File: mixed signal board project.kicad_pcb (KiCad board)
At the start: 4 copper layers, 70.4 x 72.2 mm, 189 parts, among them J101 USB_B_Mini, J102 Conn_01x06_Pin, J201 8P8C_Shielded, J301 Conn_01x04_Pin, J401 AudioJack2_Ground, J402 Conn_01x04_Pin, J403 Screw_Terminal_01x03, J501 USB_B_Mini, J701 Conn_01x02_Socket, J801 Conn_01x02_Socket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

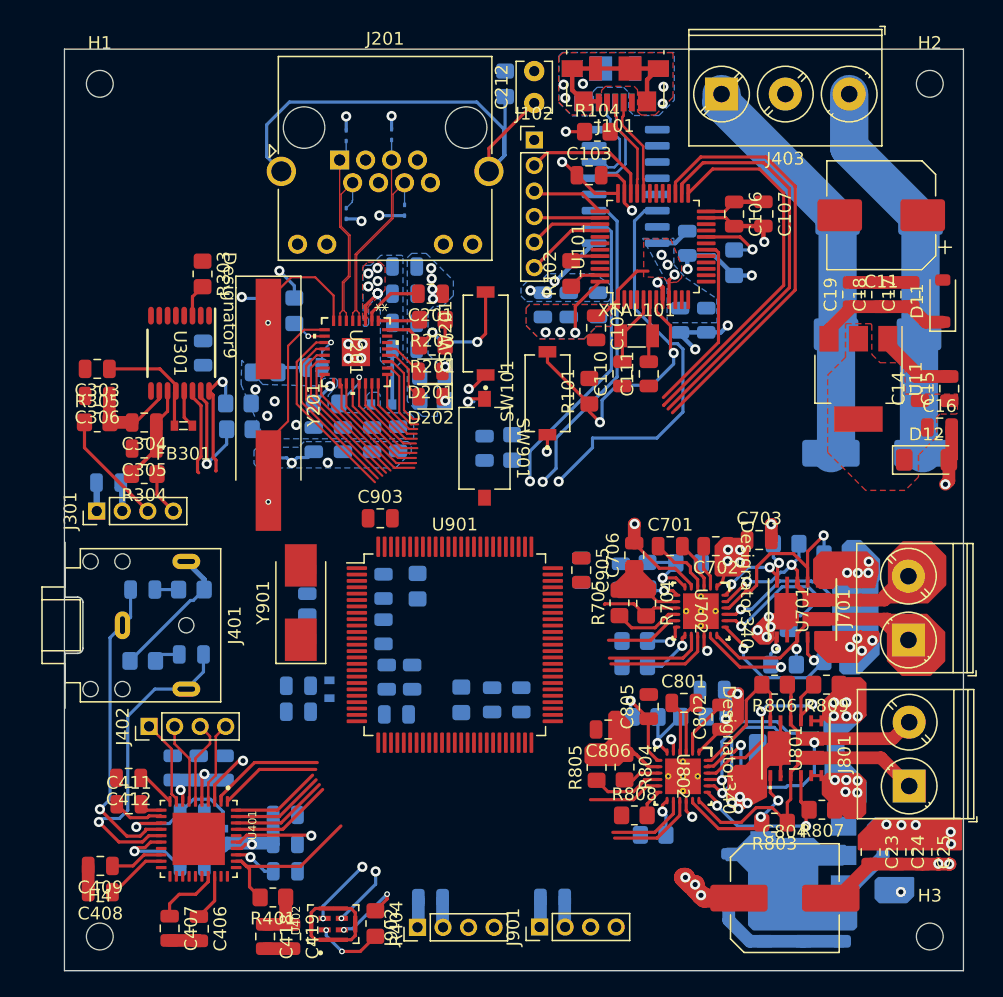
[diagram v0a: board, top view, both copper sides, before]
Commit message: ADC layout reworked, analog and digital ground reworked, other blocks layout have to rework :( ...
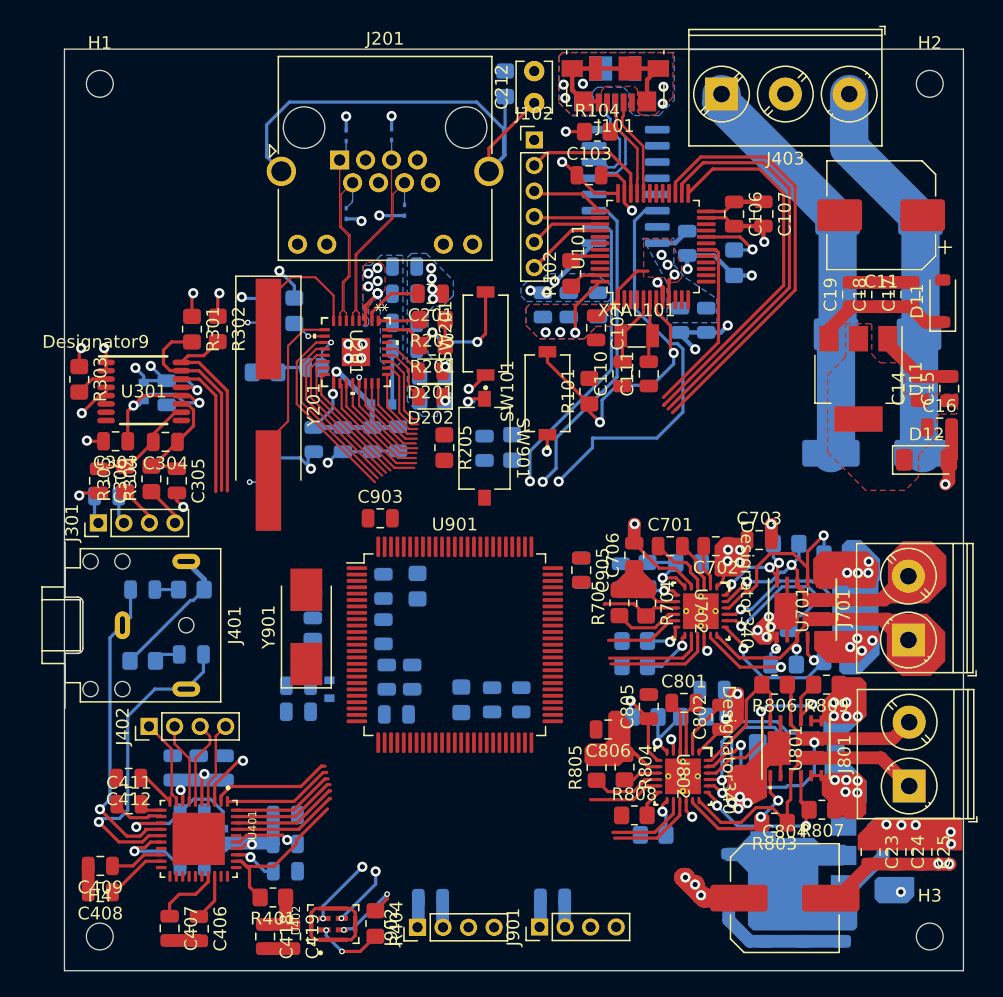
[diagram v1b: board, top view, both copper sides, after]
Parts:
- FB301: moved to B.Cu
- R205, R301, R302: moved to F.Cu
- moved R303 12.7 mm to (84.8, 83.3)
- moved R205 9.89 mm to (113.3, 88.7), turned to -90 degrees
- moved R301 8.68 mm to (93.6, 79.4), turned to -90 degrees
- moved C306 6.65 mm to (86.3, 91.3), turned to -90 degrees
- moved R302 6.06 mm to (95.6, 79.4), turned to -90 degrees
- moved C303 5.85 mm to (87.6, 88.2)
- moved R305 4.94 mm to (88.3, 91.2), turned to 90 degrees
- moved C302 4.22 mm to (91.6, 84.4), turned to -90 degrees
- moved U301 4.13 mm to (89.8, 84.3), turned to 0 degrees
- moved FB301 4.11 mm to (89.8, 84.3), turned to -90 degrees
- moved C305 3.60 mm to (92.4, 91.3), turned to -90 degrees
- moved C304 2.25 mm to (91.5, 88.2)
- moved C913 1.96 mm to (103.0, 104.7)
- moved Y901 1.96 mm to (102.5, 102.7)
- moved C912 1.96 mm to (103.0, 101.1)
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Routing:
- net +3V3: track 64.4 -> 90.1 mm, vias 18 -> 21
- net GND: track 220.2 -> 234.8 mm, vias 46 -> 51
- net /ADC/SDA_ADC: track 9.43 -> 16.8 mm, vias 1 -> 0
- net /ADC/SCK_ADC: track 9.65 -> 15.9 mm, vias 1 -> 0
- net Net-(U301-AVDD): track 9.13 -> 15.1 mm, vias 0 -> 2
- net /ADC/AIN1_ADC: track 9.00 -> 3.24 mm
- net /ADC/~{DRDY}_ADC: track 6.84 -> 10.8 mm
- net /Ethernet/ETH_INT: track 10.4 -> 7.70 mm
- net /Ethernet/ETH_XO: track 10.7 -> 12.3 mm
- net Net-(U301-AIN0): track 7.68 -> 9.08 mm
- net Net-(U301-AIN1): track 7.34 -> 8.63 mm
- net /DAC adn MIC/LRCK_DAC: track 7.12 -> 8.22 mm
- net /DAC adn MIC/SDIN_DAC: track 7.46 -> 8.39 mm
- net /DAC adn MIC/SDA_DAC: track 7.96 -> 8.73 mm
- net /DAC adn MIC/SCLK_DAC: track 7.76 -> 8.44 mm

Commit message: critical nets coloured,some tracks rerouted, section 9 completed.
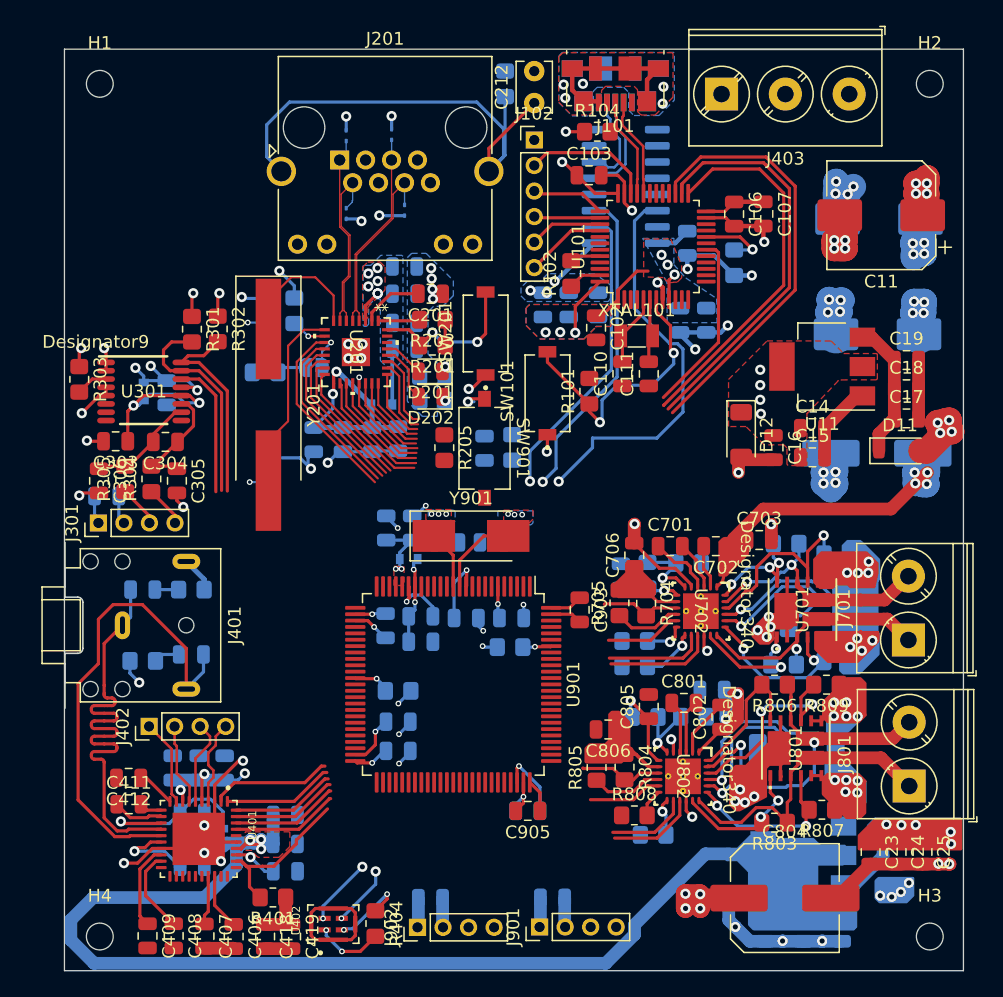
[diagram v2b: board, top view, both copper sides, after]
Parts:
- moved C905 19.3 mm to (119.9, 117.2), turned to 180 degrees
- moved C917 19.3 mm to (119.9, 117.2), turned to 180 degrees
- moved C903 17.2 mm to (124.0, 101.4), turned to -90 degrees
- moved C902 16.0 mm to (108.8, 95.0), turned to 90 degrees
- moved C901 15.2 mm to (110.8, 95.0), turned to 90 degrees
- moved C912 14.9 mm to (117.1, 96.1), turned to 0 degrees
- moved Y901 14.7 mm to (115.4, 95.6), turned to 0 degrees
- moved D12 14.7 mm to (136.6, 87.7), turned to -90 degrees
- moved C913 13.5 mm to (113.5, 96.1), turned to 180 degrees
- moved C16 13.1 mm to (139.1, 88.7), turned to -90 degrees
- moved D11 12.2 mm to (149.1, 89.0), turned to 0 degrees
- moved C15 12.0 mm to (142.2, 89.5), turned to 0 degrees
- moved FB901 11.9 mm to (110.6, 97.4), turned to 0 degrees
- moved C910 10.4 mm to (109.7, 112.5), turned to 0 degrees
- moved C904 10.3 mm to (118.6, 102.0), turned to 0 degrees
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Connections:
- C901 pad 1: Net-(U901-VDDA) -> /STM32F407/VDDA
- C902 pad 1: Net-(U901-VDDA) -> /STM32F407/VDDA
- FB901 pad 1: Net-(U901-VDDA) -> /STM32F407/VDDA
- U702 pad 25: (no net) -> GND
- U802 pad 25: (no net) -> GND
- U901 pad 21: +3V3 -> /STM32F407/VDDA
- U901 pad 22: Net-(U901-VDDA) -> /STM32F407/VDDA
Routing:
- net +1V8: track 9.39 -> 84.9 mm, vias 1 -> 3
- net +3V3: track 90.1 -> 117.7 mm, vias 21 -> 32
- net +12V: track 59.0 -> 80.4 mm, vias 18 -> 38
- net GND: track 234.8 -> 252.0 mm, vias 51 -> 85
- net Net-(U401-HP/LINE_OUTA): track 24.5 -> 37.8 mm, vias 1 -> 0
- net Net-(U401-HP/LINE_OUTB): track 24.2 -> 37.4 mm, vias 1 -> 0
- net Net-(U901-PH0): track 0.00 -> 6.65 mm, vias 0 -> 3
- net Net-(U901-VCAP_2): track 0.00 -> 5.52 mm, vias 0 -> 1
- net /STM32F407/VDDA: track 0.00 -> 5.11 mm, vias 0 -> 2
- net Net-(U901-PH1): track 0.00 -> 4.58 mm, vias 0 -> 3
- net Net-(U901-VCAP_1): track 0.00 -> 4.08 mm, vias 0 -> 1
- net /Motor_Driver1/nFAULT: track 2.90 -> 6.55 mm
- net Net-(U901-PB2): track 0.00 -> 2.94 mm, vias 0 -> 1
- net Net-(U401-FILT_P): track 4.18 -> 6.67 mm
- net /DAC adn MIC/VA: track 22.2 -> 24.5 mm
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- added copper zone on F.Cu, net +1V8
- added copper zone on F.Cu, net /STM32F407/VDDA
- added copper zone on B.Cu, net Net-(U901-PH0)
- added copper zone on F.Cu, net Net-(U901-PH0)
- added copper zone on B.Cu, net Net-(U901-PH1)
- added copper zone on F.Cu, net Net-(U901-PH1)

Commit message: ethernet PHY tracks connected to MCU, reset pin left.
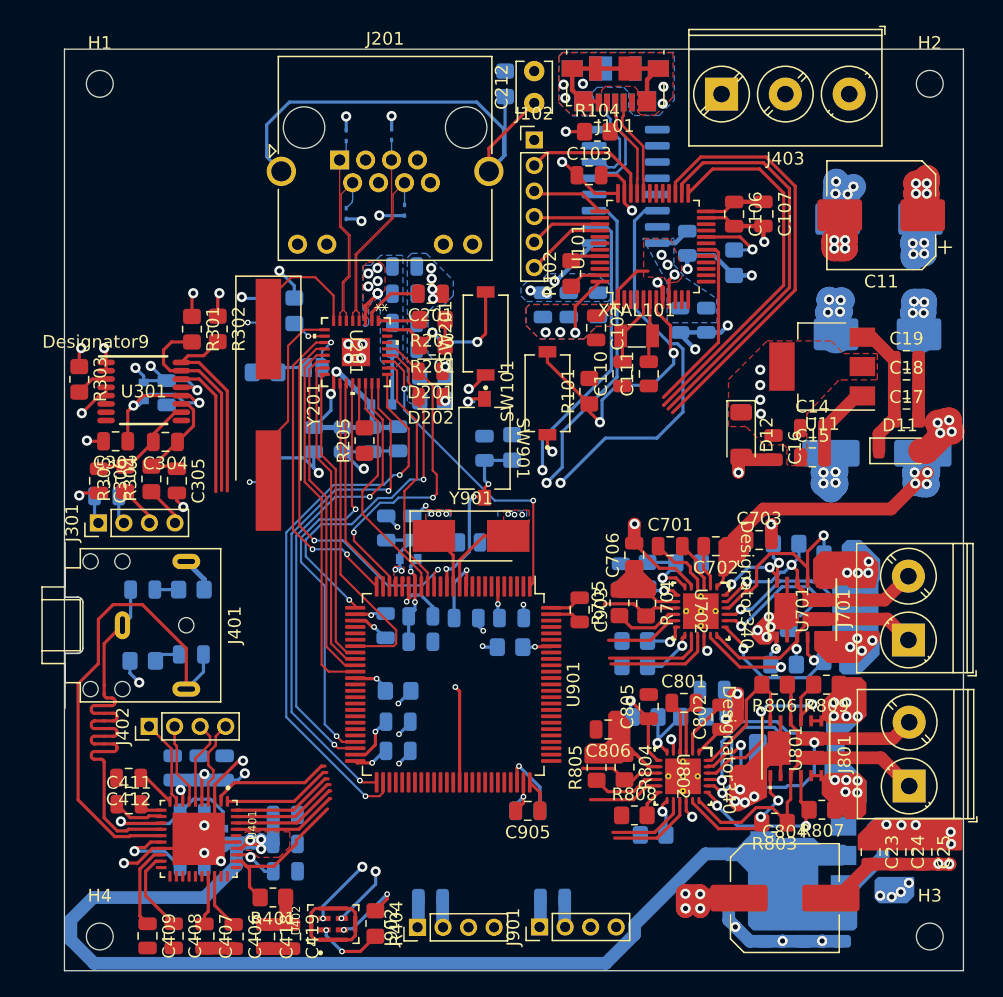
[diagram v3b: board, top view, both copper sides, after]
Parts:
- moved R205 6.27 mm to (107.1, 88.2), turned to 90 degrees
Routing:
- net /Ethernet/ETH_TX_D1: track 5.63 -> 45.2 mm, vias 0 -> 2
- net /Ethernet/ETH_TX_D0: track 5.64 -> 40.9 mm, vias 0 -> 2
- net /Ethernet/ETH_TX_EN: track 6.32 -> 36.0 mm, vias 0 -> 2
- net /Ethernet/ETH_RX_ER: track 8.29 -> 33.6 mm, vias 0 -> 2
- net /Ethernet/ETH_COL: track 4.60 -> 29.4 mm, vias 0 -> 2
- net /Ethernet/ETH_CRS: track 3.18 -> 26.7 mm, vias 0 -> 2
- net /Ethernet/ETH_TX_D3: track 6.08 -> 24.6 mm, vias 0 -> 2
- net /Ethernet/ETH_MDC: track 13.8 -> 29.8 mm, vias 0 -> 2
- net /Ethernet/ETH_RX_DV: track 9.61 -> 25.5 mm
- net /Ethernet/ETH_RX_D3: track 12.9 -> 28.7 mm
- net /Ethernet/ETH_RX_D2: track 11.9 -> 26.6 mm
- net /STM32F407/NTRST_F407: track 14.2 -> 28.6 mm, vias 0 -> 3
- net /Ethernet/ETH_RX_D1: track 11.0 -> 25.0 mm
- net /Ethernet/ETH_TX_D2: track 5.91 -> 19.6 mm
- net /Ethernet/ETH_RX_D0: track 11.4 -> 23.4 mm
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
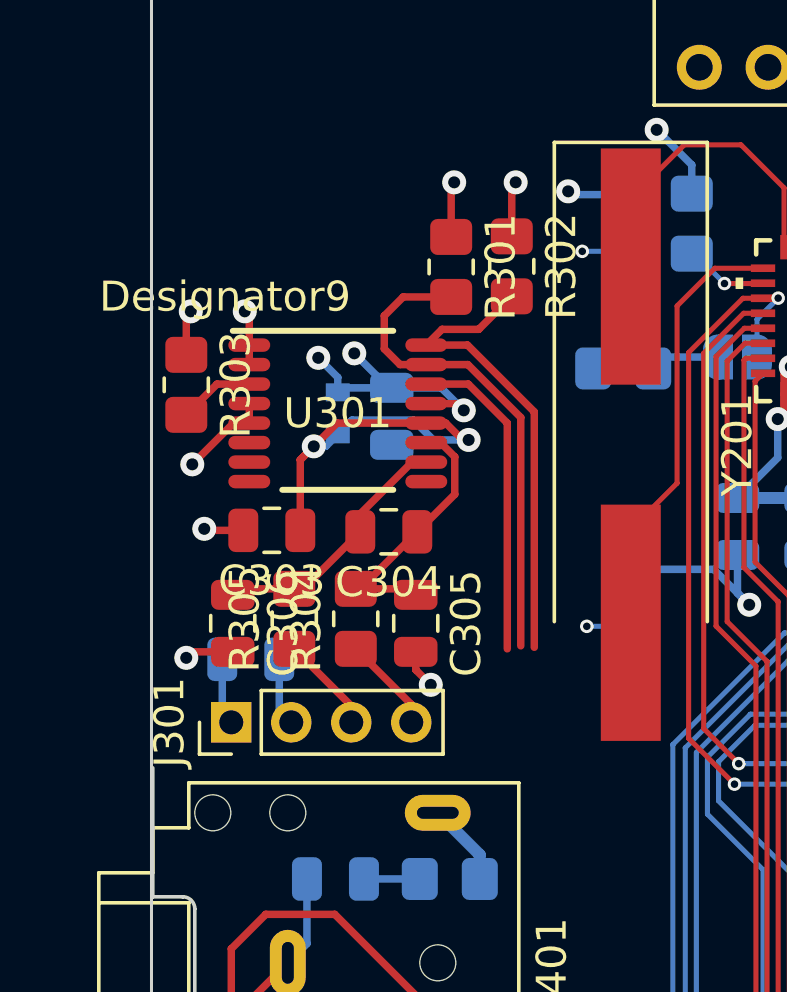
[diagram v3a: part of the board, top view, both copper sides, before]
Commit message: I2C pins that is on ADC and DAC corrected
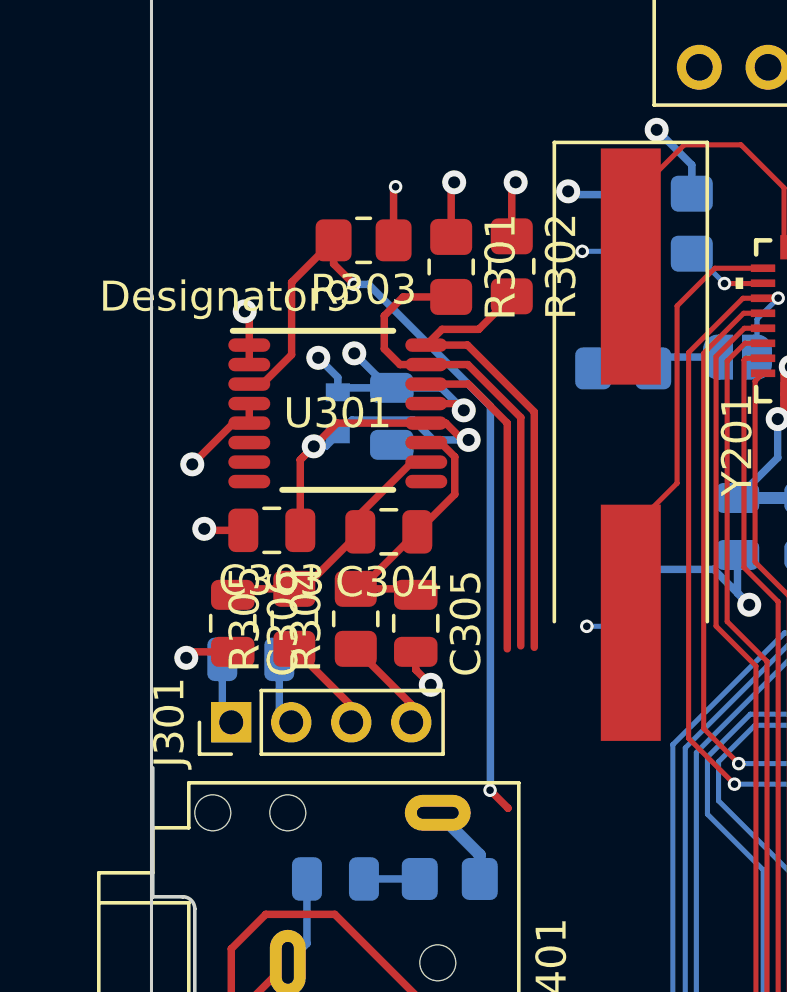
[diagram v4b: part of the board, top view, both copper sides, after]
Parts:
- moved R303 7.62 mm to (90.7, 78.5), turned to 180 degrees
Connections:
- R301 pad 2: /ADC/SDA_ADC -> /ADC/SDA
- R302 pad 2: /ADC/SCK_ADC -> /ADC/SCL
- U301 pad 15: /ADC/SDA_ADC -> /ADC/SDA
- U301 pad 16: /ADC/SCK_ADC -> /ADC/SCL
- U401 pad 1: /DAC adn MIC/SDA_DAC -> /ADC/SDA
- U401 pad 2: /DAC adn MIC/SCL_DAC -> /ADC/SCL
- U901 pad 92: /DAC adn MIC/SCL_DAC -> /ADC/SCL
- U901 pad 93: /DAC adn MIC/SDA_DAC -> /ADC/SDA
- U901 pad 95: /ADC/SCK_ADC -> unconnected-(U901-PB8-Pad95)
- U901 pad 96: /ADC/SDA_ADC -> unconnected-(U901-PB9-Pad96)
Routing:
- net /ADC/SDA: track 0.00 -> 25.6 mm
- net /ADC/SCL: track 0.00 -> 25.4 mm
- net /ADC/RESET_ADC: track 2.52 -> 27.8 mm, vias 0 -> 2
- net /ADC/SDA_ADC: track 16.8 -> 0.00 mm
- net /ADC/SCK_ADC: track 15.9 -> 0.00 mm
- net /DAC adn MIC/SCL_DAC: track 9.53 -> 0.00 mm
- net /DAC adn MIC/SDA_DAC: track 8.73 -> 0.00 mm
